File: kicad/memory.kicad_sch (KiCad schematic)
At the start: 8 parts, among them U28 AS6C4008-55PCN, U29 27C128, U30 74HC00, U40 AS6C4008-55PCN

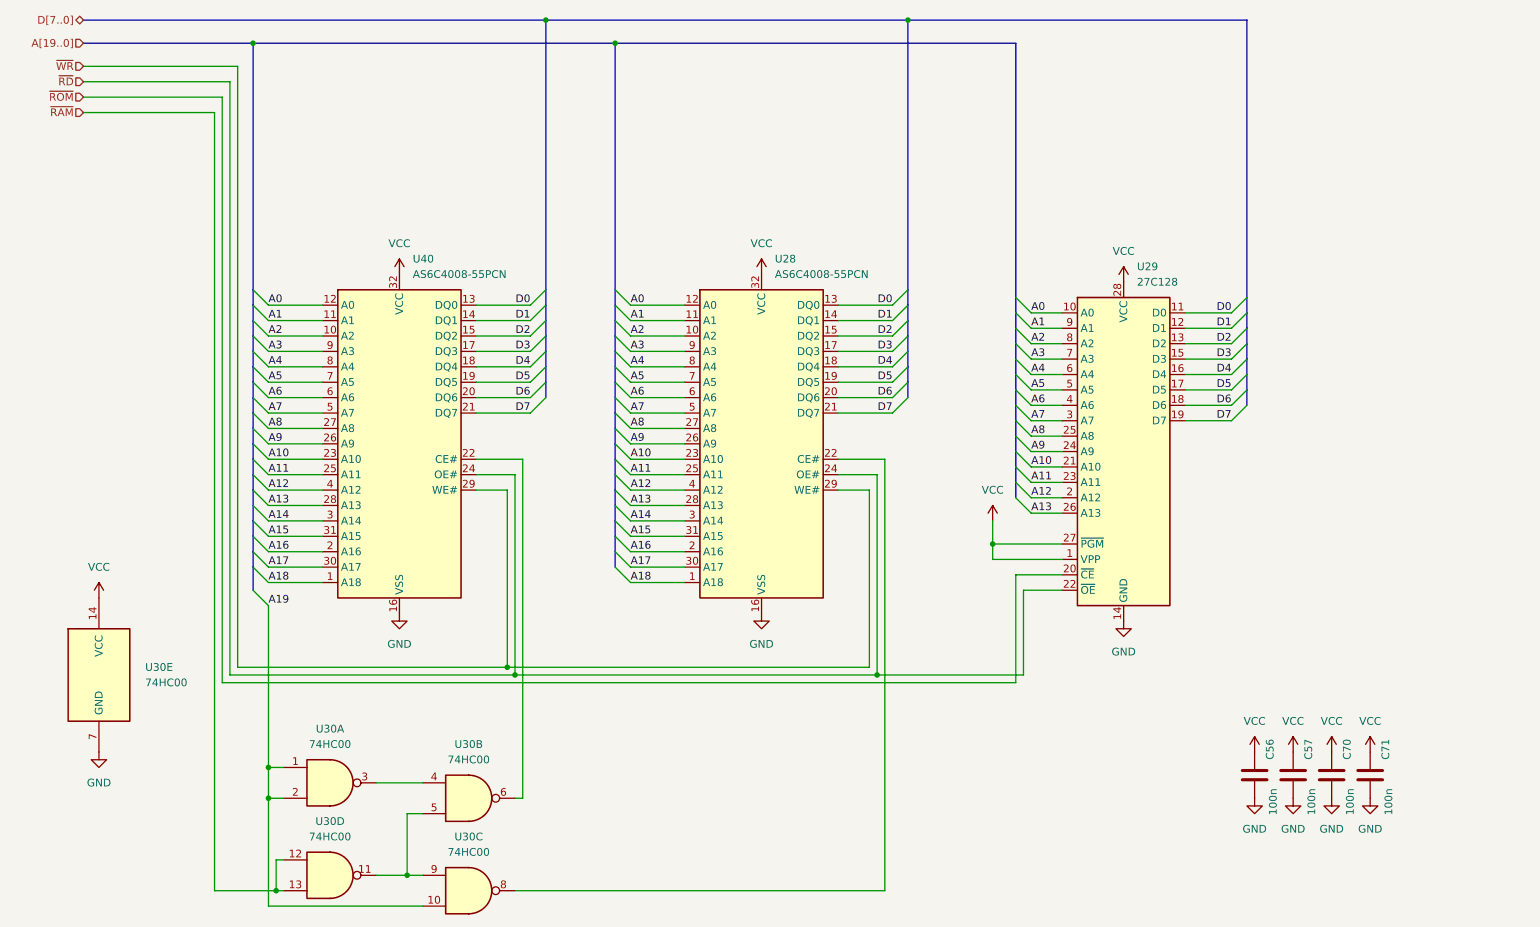
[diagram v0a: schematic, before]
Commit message: hw: simplify logic, replace some SSI with GALs
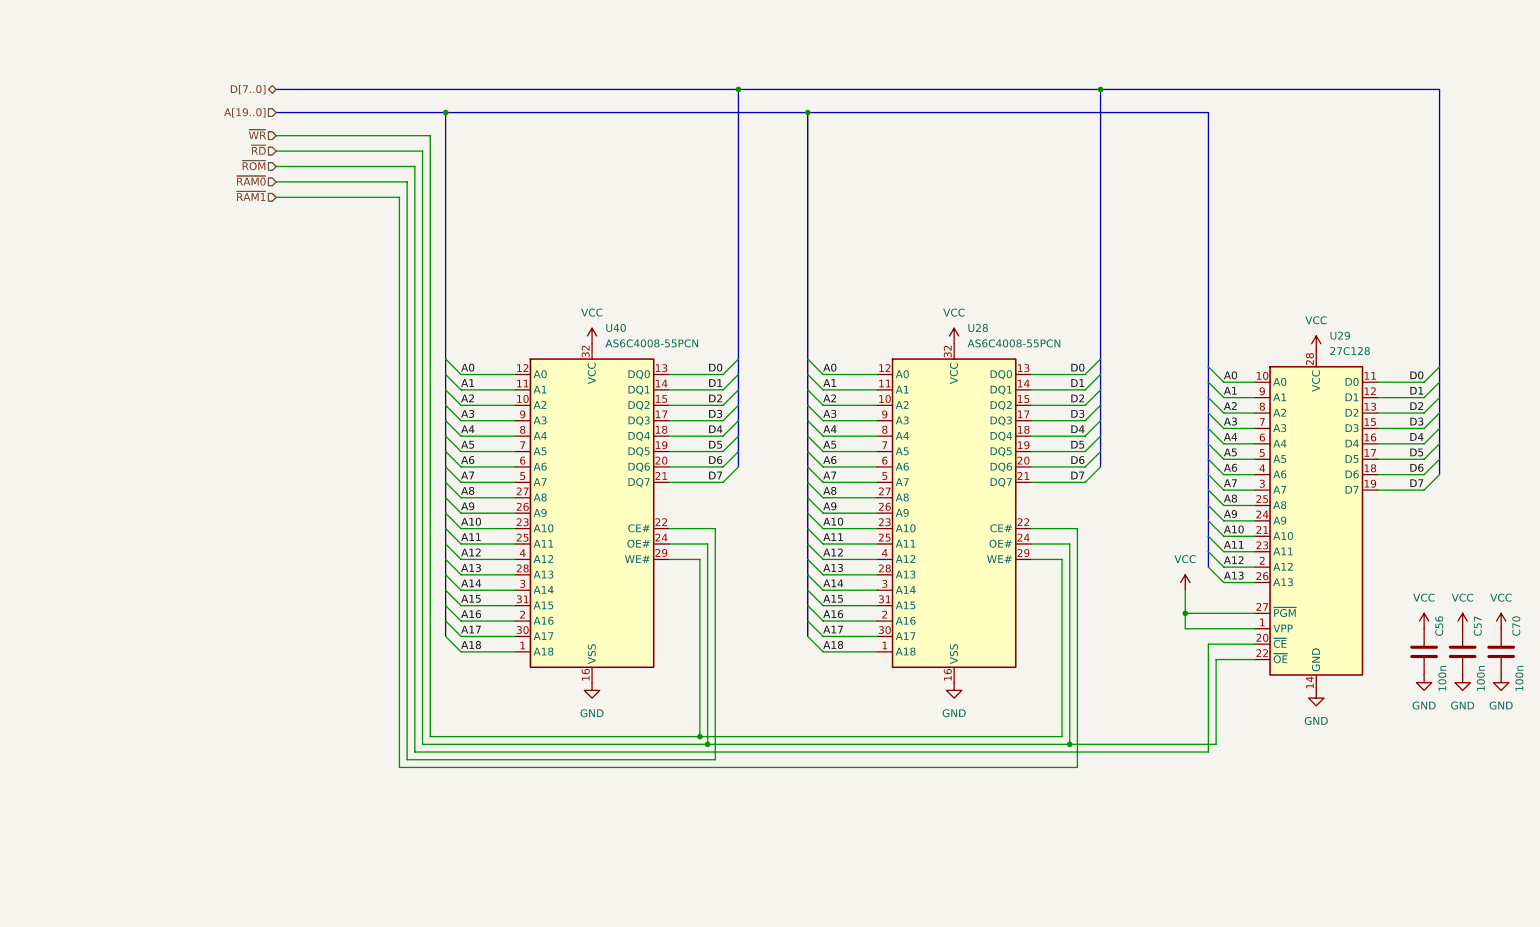
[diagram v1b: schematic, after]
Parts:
- removed C71: 100n, Capacitor_THT:C_Disc_D5.0mm_W2.5mm_P2.50mm, symbol Device:C
- removed U30: 74HC00, Package_DIP:DIP-14_W7.62mm, symbol 74xx:74HC00
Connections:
- net ~{RAM0}: now reaches U40.22 (CE#)
- net ~{RAM1}: now reaches U28.22 (CE#)
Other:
- moved on the sheet: C56, C57, C70, U28, U29, U40

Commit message: hw: finish schematic, start routing
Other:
- company: (none) -> A.K.
- title: (none) -> Memory
- moved on the sheet: C56, C57, C70, U28, U29, U40

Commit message: hw: finish routing
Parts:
- U28, U40: value AS6C4008-55PCN -> AS6C4008
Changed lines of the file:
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@@
 			)
 		)
-		(property "Value" "AS6C4008-55PCN"
+		(property "Value" "AS6C4008"
 			(at 103.7941 67.31 0)
 			(effects
@@
 			)
 		)
-		(property "Value" "AS6C4008-55PCN"
+		(property "Value" "AS6C4008"
 			(at 163.4841 67.31 0)
 			(effects
